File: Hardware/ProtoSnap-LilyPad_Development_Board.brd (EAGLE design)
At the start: 104.1 x 72.4 mm, 158 parts, among them M1 MOTORSMD, U1 ATMEGA328, U2 MCP9700, U3 TEMT6000, U4 MCP73831, Y1 8MHz

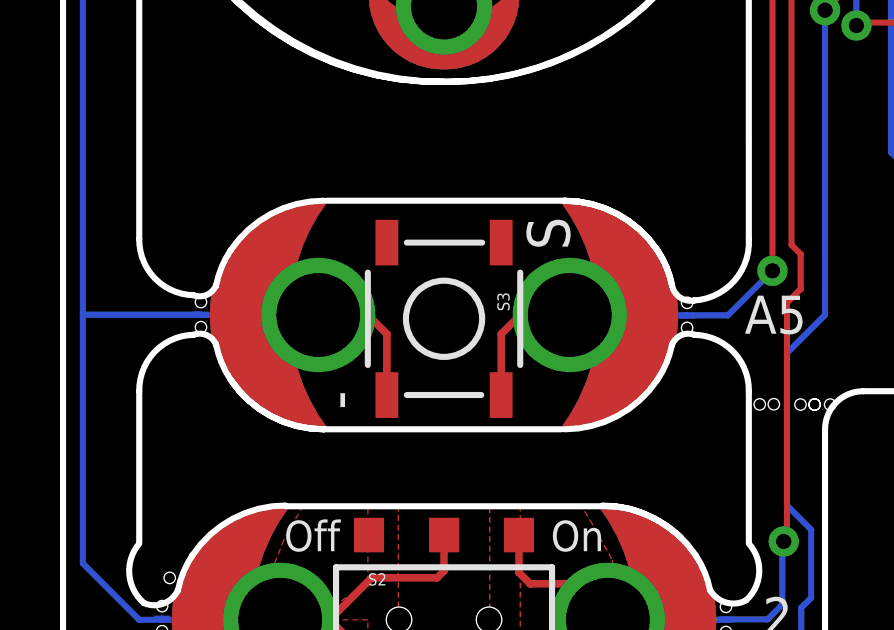
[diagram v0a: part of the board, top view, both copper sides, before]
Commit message: Updated momentary buttons to new package
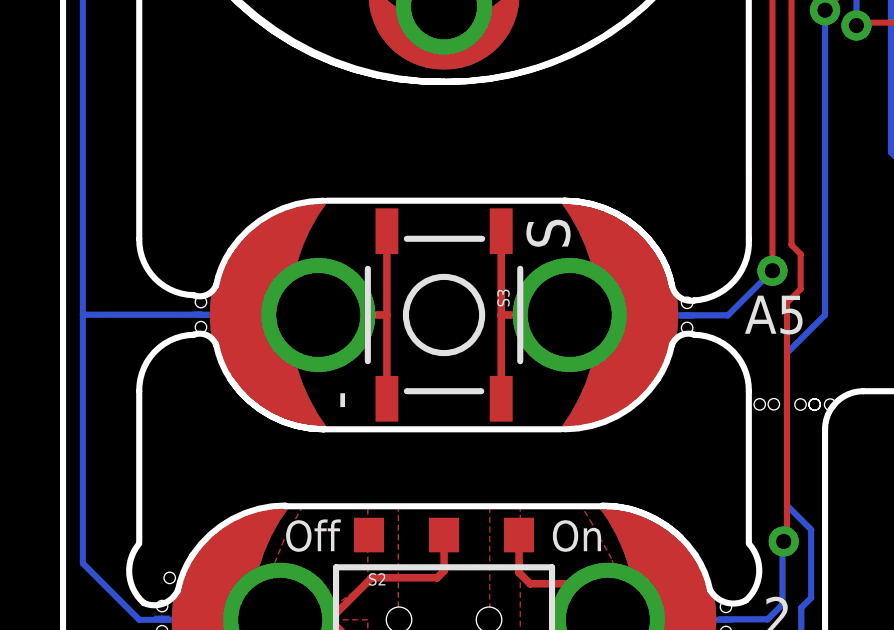
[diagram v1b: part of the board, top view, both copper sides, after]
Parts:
- S3: device SparkFun:TACTILE_SWITCH_SMD -> SparkFun-Electromechanical:TACTILE-SWITCH-SMD
- S4: device Testing:TACTILE-SWITCH-SMD-ALT01 -> SparkFun-Electromechanical:TACTILE-SWITCH-SMD
- moved S3 0.13 mm to (12.7, 19.1)
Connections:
- net A5: now also S3.1
- net GND: now also S3.3
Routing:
- net GND: track 470.7 -> 474.0 mm
- net A5: track 106.0 -> 109.3 mm
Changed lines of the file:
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@@
 <layer number="27" name="tValues" color="7" fill="1" visible="no" active="yes"/>
 <layer number="28" name="bValues" color="7" fill="1" visible="no" active="yes"/>
-<layer number="29" name="tStop" color="5" fill="1" visible="no" active="yes"/>
+<layer number="29" name="tStop" color="5" fill="1" visible="yes" active="yes"/>
 <layer number="30" name="bStop" color="7" fill="6" visible="no" active="yes"/>
 <layer number="31" name="tCream" color="7" fill="4" visible="no" active="yes"/>
@@
 <layer number="54" name="bGND_GNDA" color="1" fill="9" visible="no" active="no"/>
 <layer number="56" name="wert" color="7" fill="1" visible="no" active="yes"/>
+<layer number="57" name="tCAD" color="7" fill="1" visible="no" active="no"/>
 <layer number="91" name="Nets" color="2" fill="1" visible="no" active="no"/>
 <layer number="92" name="Busses" color="1" fill="1" visible="no" active="no"/>
@@
 <layer number="97" name="Info" color="7" fill="1" visible="no" active="no"/>
 <layer number="98" name="Guide" color="6" fill="1" visible="no" active="no"/>
+<layer number="99" name="SpiceOrder" color="7" fill="1" visible="no" active="no"/>
 <layer number="100" name="Muster" color="7" fill="1" visible="no" active="no"/>
 <layer number="101" name="Patch_Top" color="12" fill="4" visible="no" active="yes"/>
@@
 <layer number="108" name="tplace-old" color="10" fill="1" visible="no" active="yes"/>
 <layer number="109" name="ref-old" color="11" fill="1" visible="no" active="yes"/>
+<layer number="110" name="fp0" color="7" fill="1" visible="yes" active="yes"/>
+<layer number="111" name="LPC17xx" color="7" fill="1" visible="yes" active="yes"/>
+<layer number="112" name="tSilk" color="7" fill="1" visible="yes" active="yes"/>
 <layer number="116" name="Patch_BOT" color="9" fill="4" visible="no" active="yes"/>
 <layer number="121" name="_tsilk" color="7" fill="1" visible="no" active="yes"/>
 <layer number="122" name="_bsilk" color="7" fill="1" visible="no" active="yes"/>
+<layer number="123" name="tTestmark" color="7" fill="1" visible="yes" active="yes"/>
+<layer number="124" name="bTestmark" color="7" fill="1" visible="yes" active="yes"/>
 <layer number="125" name="_tNames" color="7" fill="1" visible="no" active="yes"/>
+<layer number="126" name="_bNames" color="7" fill="1" visible="yes" active="yes"/>
+<layer number="127" name="_tValues" color="7" fill="1" visible="yes" active="yes"/>
+<layer number="128" name="_bValues" color="7" fill="1" visible="yes" active="yes"/>
+<layer number="131" name="tAdjust" color="7" fill="1" visible="yes" active="yes"/>
+<layer number="132" name="bAdjust" color="7" fill="1" visible="yes" active="yes"/>
 <layer number="144" name="Drill_legend" color="7" fill="1" visible="no" active="yes"/>
+<layer number="150" name="Notes" color="7" fill="1" visible="yes" active="yes"/>
 <layer number="151" name="HeatSink" color="7" fill="1" visible="no" active="yes"/>
+<layer number="152" name="_bDocu" color="7" fill="1" visible="yes" active="yes"/>
+<layer number="153" name="FabDoc1" color="7" fill="1" visible="yes" active="yes"/>
+<layer number="154" name="FabDoc2" color="7" fill="1" visible="yes" active="yes"/>
+<layer number="155" name="FabDoc3" color="7" fill="1" visible="yes" active="yes"/>
 <layer number="199" name="Contour" color="7" fill="1" visible="no" active="yes"/>
 <layer number="200" name="200bmp" color="1" fill="10" visible="no" active="no"/>
@@
 <layer number="223" name="223bmp" color="24" fill="1" visible="no" active="no"/>
 <layer number="224" name="224bmp" color="25" fill="1" visible="no" active="no"/>
+<layer number="248" name="Housing" color="7" fill="1" visible="yes" active="yes"/>
+<layer number="249" name="Edge" color="7" fill="1" visible="yes" active="yes"/>
 <layer number="250" name="Descript" color="3" fill="1" visible="no" active="no"/>
 <layer number="251" name="SMDround" color="12" fill="11" visible="no" active="no"/>
@@
 <element name="SLIDEON" library="LilyPad-Wearables" package="PETAL-MEDIUM-2SIDE" value="SEWTAP8" x="17.907" y="8.89" rot="R90"/>
 <element name="LOGO1" library="LilyPad-Wearables" package="LOGO-L" value="LOGO-LPL" x="12.7" y="8.89" rot="MR0"/>
-<element name="S3" library="SparkFun" package="TACTILE_SWITCH_SMD" value="" x="12.7" y="18.923" rot="R270"/>
 <element name="BUTTONS" library="LilyPad-Wearables" package="PETAL-MEDIUM-2SIDE" value="SEWTAP8" x="16.637" y="19.05" rot="R90"/>
 <element name="BUTTON-" library="LilyPad-Wearables" package="PETAL-MEDIUM-2SIDE" value="SEWTAP8" x="8.763" y="19.05" rot="R270"/>
@@
 <element name="R12" library="SparkFun" package="0603-RES" value="330" x="44.178" y="39.9901" rot="R270"/>
 <element name="U4" library="SparkFun" package="SOT23-5" value="MCP73831" x="40.324" y="39.9901" rot="R180"/>
-<element name="S4" library="Testing" package="TACTILE-SWITCH-SMD-ALT01" value="Reset" x="41.0701" y="55.9901" rot="R90"/>
+<element name="S4" library="SparkFun-Electromechanical" package="TACTILE-SWITCH-SMD" value="Reset" x="41.0701" y="55.9901" rot="R90"/>
 <element name="PP-MISO" library="SparkFun" package="PAD.03X.05" value="" x="57.0701" y="41.9901" rot="MR0"/>
 <element name="PP-SCK" library="SparkFun" package="PAD.03X.05" value="" x="59.0701" y="46.9901" rot="MR0"/>
@@
 <element name="FRAME2" library="SparkFun-Aesthetics" package="CREATIVE_COMMONS" value="FRAME-LEDGER" x="24.13" y="-8.89"/>
 <element name="D5" library="SparkFun-DiscreteSemi" package="SMA-DIODE" value="B340A" x="42.418" y="36.449"/>
+<element name="S3" library="SparkFun-Electromechanical" package="TACTILE-SWITCH-SMD" value="" x="12.7" y="19.05" rot="R270"/>
 </elements>
 <signals>
@@
 <contactref element="VIBE-" pad="1"/>
 <contactref element="U$42" pad="P$1"/>
-<contactref element="S3" pad="4"/>
 <contactref element="BUTTON-" pad="1"/>
 <contactref element="U$44" pad="P$1"/>
@@
 <wire x1="91.44" y1="59.52" x2="90.889" y2="59.52" width="0.254" layer="1"/>
 <wire x1="90.889" y1="59.52" x2="90.639" y2="59.27" width="0.254" layer="1"/>
-<wire x1="10.795" y1="18.415" x2="10.795" y2="16.383" width="0.254" layer="1"/>
-<wire x1="10.16" y1="19.05" x2="10.795" y2="18.415" width="0.254" layer="1"/>
 <wire x1="8.509" y1="19.05" x2="10.16" y2="19.05" width="0.254" layer="1"/>
 <wire x1="4.6101" y1="19.05" x2="8.509" y2="19.05" width="0.2032" layer="16"/>
@@
 <wire x1="37.564" y1="53.1961" x2="39.1651" y2="53.1961" width="0.254" layer="1"/>
 <wire x1="39.1651" y1="58.7841" x2="39.1651" y2="53.1961" width="0.254" layer="1"/>
+<contactref element="S3" pad="4"/>
+<contactref element="S3" pad="3"/>
+<wire x1="10.795" y1="19.05" x2="10.795" y2="21.844" width="0.254" layer="1"/>
+<wire x1="10.16" y1="19.05" x2="10.795" y2="19.05" width="0.254" layer="1"/>
+<wire x1="10.795" y1="19.05" x2="10.795" y2="16.256" width="0.254" layer="1"/>
 </signal>
 <signal name="VCC" class="1">
@@
 <contactref element="U1" pad="28"/>
 <contactref element="U$40" pad="P$1"/>
-<contactref element="S3" pad="2"/>
 <contactref element="BUTTONS" pad="1"/>
 <contactref element="U$8" pad="P$1"/>
@@
 <wire x1="52.37" y1="48.9901" x2="52.3701" y2="50.4901" width="0.254" layer="1"/>
 <wire x1="52.4701" y1="48.8901" x2="52.37" y2="48.9901" width="0.254" layer="1"/>
-<wire x1="14.605" y1="16.383" x2="14.605" y2="18.415" width="0.254" layer="1"/>
-<wire x1="14.605" y1="18.415" x2="15.24" y2="19.05" width="0.254" layer="1"/>
 <wire x1="15.24" y1="19.05" x2="16.891" y2="19.05" width="0.254" layer="1"/>
 <wire x1="16.891" y1="19.05" x2="16.891" y2="19.0373" width="0.2032" layer="16"/>
@@
 <wire x1="48.3399" y1="51.9901" x2="49.657" y2="50.673" width="0.254" layer="16"/>
 <wire x1="49.657" y1="50.673" x2="49.657" y2="50.165" width="0.254" layer="16"/>
+<contactref element="S3" pad="1"/>
+<contactref element="S3" pad="2"/>
+<wire x1="14.605" y1="19.05" x2="14.605" y2="21.844" width="0.254" layer="1"/>
+<wire x1="15.24" y1="19.05" x2="14.605" y2="19.05" width="0.254" layer="1"/>
+<wire x1="14.605" y1="19.05" x2="14.605" y2="16.256" width="0.254" layer="1"/>
 </signal>
 <signal name="STAT">

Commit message: Replaced resonator device to SparkFun-FreqCtrl.lbr
This used to be from SFE-testing-library, and now it's linked to the
"official/proven" SFE library.
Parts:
- Y1: device Testing:RESONATOR-SMD-1:1 -> SparkFun-FreqCtrl:RESONATOR-SMD
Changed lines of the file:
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@@
 <layer number="27" name="tValues" color="7" fill="1" visible="no" active="yes"/>
 <layer number="28" name="bValues" color="7" fill="1" visible="no" active="yes"/>
-<layer number="29" name="tStop" color="5" fill="1" visible="yes" active="yes"/>
+<layer number="29" name="tStop" color="5" fill="1" visible="no" active="yes"/>
 <layer number="30" name="bStop" color="7" fill="6" visible="no" active="yes"/>
 <layer number="31" name="tCream" color="7" fill="4" visible="no" active="yes"/>
@@
 <layer number="108" name="tplace-old" color="10" fill="1" visible="no" active="yes"/>
 <layer number="109" name="ref-old" color="11" fill="1" visible="no" active="yes"/>
-<layer number="110" name="fp0" color="7" fill="1" visible="yes" active="yes"/>
-<layer number="111" name="LPC17xx" color="7" fill="1" visible="yes" active="yes"/>
-<layer number="112" name="tSilk" color="7" fill="1" visible="yes" active="yes"/>
+<layer number="110" name="fp0" color="7" fill="1" visible="no" active="yes"/>
+<layer number="111" name="LPC17xx" color="7" fill="1" visible="no" active="yes"/>
+<layer number="112" name="tSilk" color="7" fill="1" visible="no" active="yes"/>
 <layer number="116" name="Patch_BOT" color="9" fill="4" visible="no" active="yes"/>
 <layer number="121" name="_tsilk" color="7" fill="1" visible="no" active="yes"/>
 <layer number="122" name="_bsilk" color="7" fill="1" visible="no" active="yes"/>
-<layer number="123" name="tTestmark" color="7" fill="1" visible="yes" active="yes"/>
-<layer number="124" name="bTestmark" color="7" fill="1" visible="yes" active="yes"/>
+<layer number="123" name="tTestmark" color="7" fill="1" visible="no" active="yes"/>
+<layer number="124" name="bTestmark" color="7" fill="1" visible="no" active="yes"/>
 <layer number="125" name="_tNames" color="7" fill="1" visible="no" active="yes"/>
-<layer number="126" name="_bNames" color="7" fill="1" visible="yes" active="yes"/>
-<layer number="127" name="_tValues" color="7" fill="1" visible="yes" active="yes"/>
-<layer number="128" name="_bValues" color="7" fill="1" visible="yes" active="yes"/>
-<layer number="131" name="tAdjust" color="7" fill="1" visible="yes" active="yes"/>
-<layer number="132" name="bAdjust" color="7" fill="1" visible="yes" active="yes"/>
+<layer number="126" name="_bNames" color="7" fill="1" visible="no" active="yes"/>
+<layer number="127" name="_tValues" color="7" fill="1" visible="no" active="yes"/>
+<layer number="128" name="_bValues" color="7" fill="1" visible="no" active="yes"/>
+<layer number="131" name="tAdjust" color="7" fill="1" visible="no" active="yes"/>
+<layer number="132" name="bAdjust" color="7" fill="1" visible="no" active="yes"/>
 <layer number="144" name="Drill_legend" color="7" fill="1" visible="no" active="yes"/>
-<layer number="150" name="Notes" color="7" fill="1" visible="yes" active="yes"/>
+<layer number="150" name="Notes" color="7" fill="1" visible="no" active="yes"/>
 <layer number="151" name="HeatSink" color="7" fill="1" visible="no" active="yes"/>
-<layer number="152" name="_bDocu" color="7" fill="1" visible="yes" active="yes"/>
-<layer number="153" name="FabDoc1" color="7" fill="1" visible="yes" active="yes"/>
-<layer number="154" name="FabDoc2" color="7" fill="1" visible="yes" active="yes"/>
-<layer number="155" name="FabDoc3" color="7" fill="1" visible="yes" active="yes"/>
+<layer number="152" name="_bDocu" color="7" fill="1" visible="no" active="yes"/>
+<layer number="153" name="FabDoc1" color="7" fill="1" visible="no" active="yes"/>
+<layer number="154" name="FabDoc2" color="7" fill="1" visible="no" active="yes"/>
+<layer number="155" name="FabDoc3" color="7" fill="1" visible="no" active="yes"/>
 <layer number="199" name="Contour" color="7" fill="1" visible="no" active="yes"/>
 <layer number="200" name="200bmp" color="1" fill="10" visible="no" active="no"/>
@@
 <layer number="223" name="223bmp" color="24" fill="1" visible="no" active="no"/>
 <layer number="224" name="224bmp" color="25" fill="1" visible="no" active="no"/>
-<layer number="248" name="Housing" color="7" fill="1" visible="yes" active="yes"/>
-<layer number="249" name="Edge" color="7" fill="1" visible="yes" active="yes"/>
+<layer number="248" name="Housing" color="7" fill="1" visible="no" active="yes"/>
+<layer number="249" name="Edge" color="7" fill="1" visible="no" active="yes"/>
 <layer number="250" name="Descript" color="3" fill="1" visible="no" active="no"/>
 <layer number="251" name="SMDround" color="12" fill="11" visible="no" active="no"/>
@@
 <element name="C2" library="SparkFun" package="EIA3528" value="47uF" x="63.34" y="46.9901" rot="R90"/>
 <element name="C3" library="SparkFun" package="0603-CAP" value="1.0uF" x="45.324" y="48.7361" rot="R90"/>
-<element name="Y1" library="Testing" package="RESONATOR-SMD-1:1" value="8MHz" x="45.424" y="44.9901" rot="R270"/>
+<element name="Y1" library="SparkFun-FreqCtrl" package="RESONATOR-SMD" value="8MHz" x="45.424" y="44.9901" rot="R270">
+<attribute name="PROD_ID" value="XTAL-08895" x="45.424" y="44.9901" size="1.778" layer="27" rot="R270" display="off"/>
+<attribute name="VALUE" value="8MHZ" x="45.424" y="44.9901" size="1.778" layer="27" rot="R270" display="off"/>
+</element>
 <element name="JP2" library="SparkFun" package="1X06-SMD" value="" x="52.07" y="58.9902" rot="R180"/>
 <element name="C4" library="SparkFun" package="0603-CAP" value="0.1uF" x="61.07" y="53.9902" rot="R270"/>

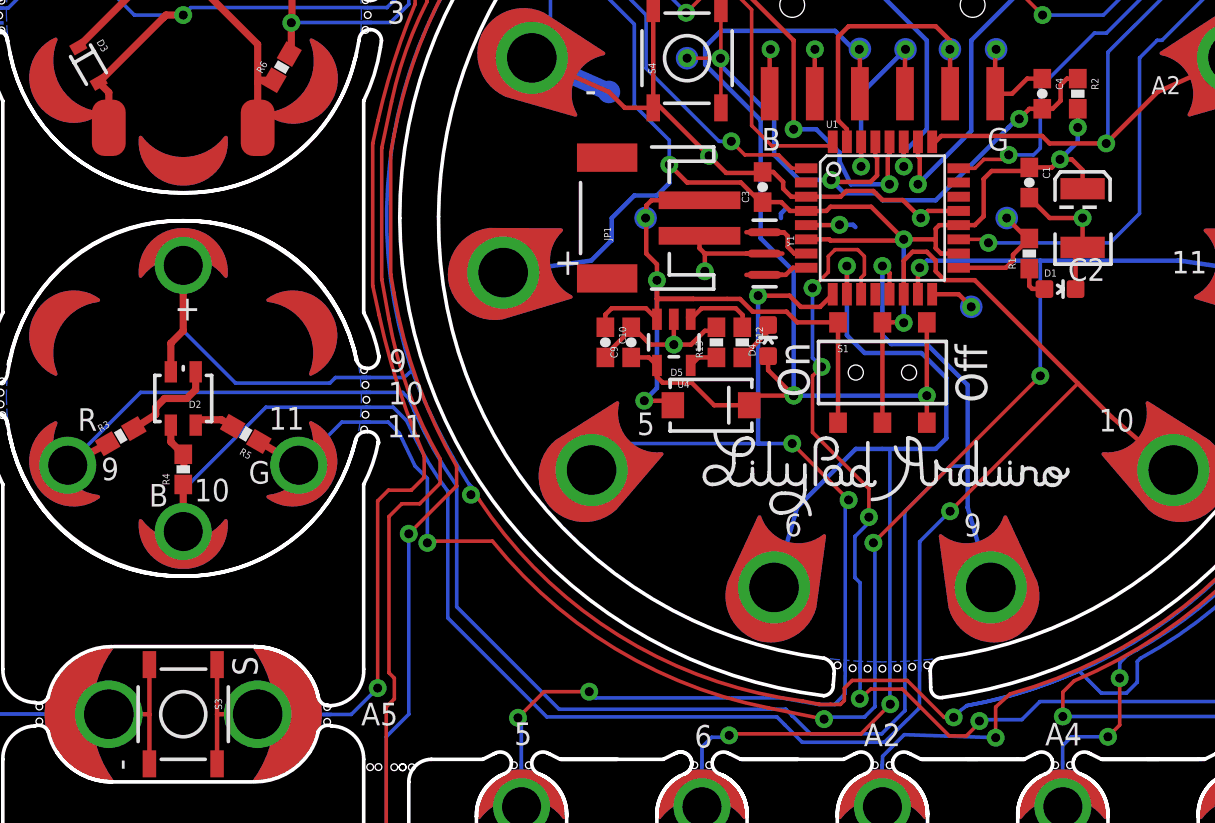
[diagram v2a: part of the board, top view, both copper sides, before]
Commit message: Schematic cleanup and a few brd part nudges
-Fixed 4 way junction in reset net.
-Moved a few vias, and parts to avoid DRC clearance errors.
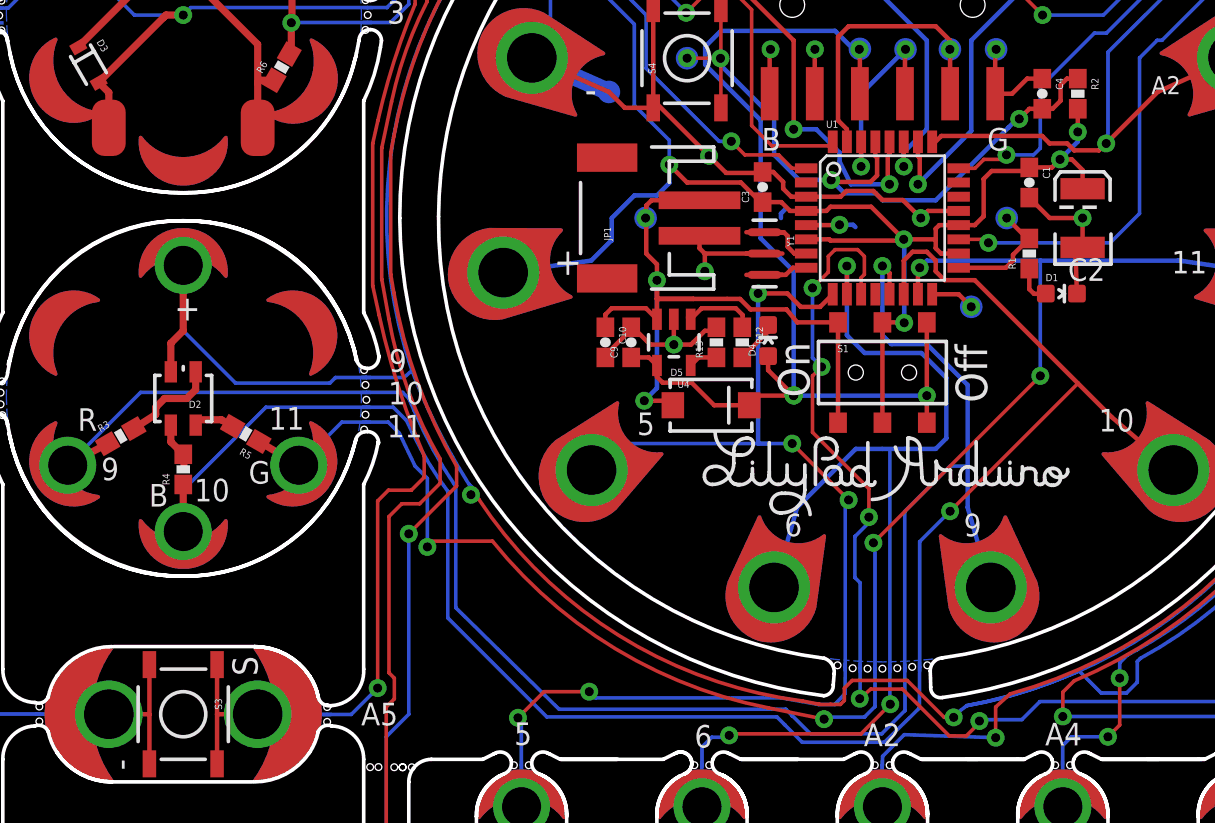
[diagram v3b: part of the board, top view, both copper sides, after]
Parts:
- moved D1 0.27 mm to (62.1, 42.7)
